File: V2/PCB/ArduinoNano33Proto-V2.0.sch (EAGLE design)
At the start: 53 parts, among them J1 RJ11, J2 RJ11, J23 455-1750-1-ND, J24 455-1750-1-ND, J26 455-1750-1-ND, J27 455-1750-1-ND, J31 455-1750-1-ND, J32 455-1750-1-ND, J38 455-1750-1-ND, J39 455-1750-1-ND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

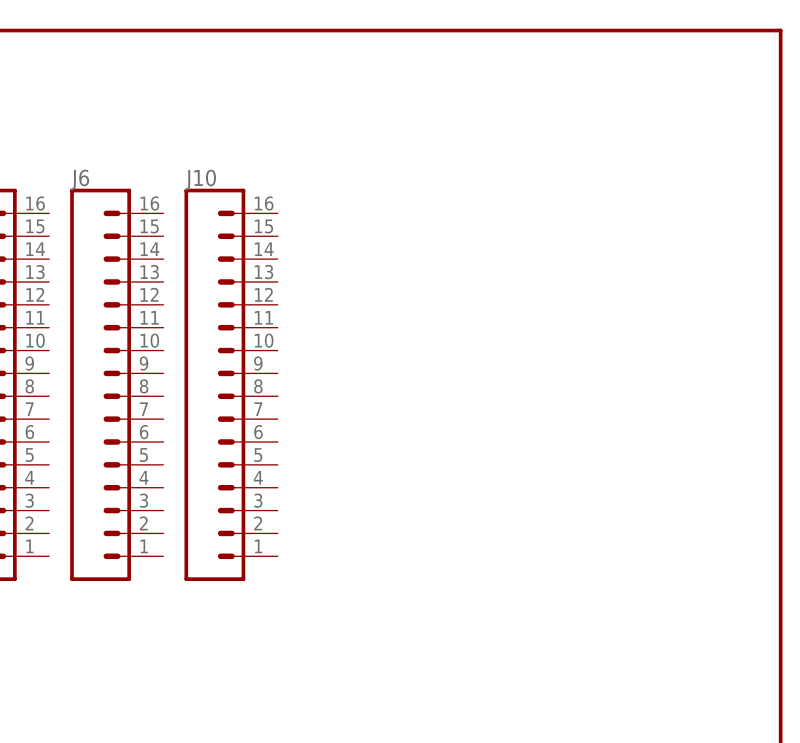
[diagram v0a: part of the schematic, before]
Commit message: Update to V2 (RJ11) board.
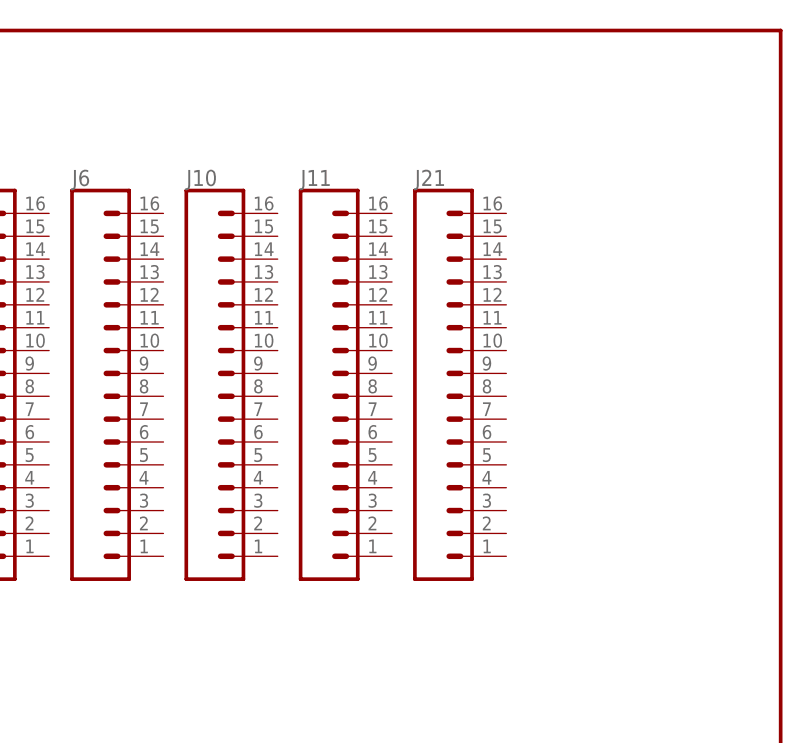
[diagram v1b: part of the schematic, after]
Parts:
- added J11, J21: (no value), SparkFun-Connectors:CONN_161X16_NO_SILK
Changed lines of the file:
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@@
 <part name="J34" library="SparkFun-Connectors" deviceset="CONN_01" device="PTH_NO_SILK_YES_STOP"/>
 <part name="J35" library="SparkFun-Connectors" deviceset="CONN_01" device="PTH_NO_SILK_YES_STOP"/>
+<part name="J11" library="SparkFun-Connectors" deviceset="CONN_16" device="1X16_NO_SILK"/>
+<part name="J21" library="SparkFun-Connectors" deviceset="CONN_16" device="1X16_NO_SILK"/>
 </parts>
 <sheets>
@@
 <instance part="J34" gate="G$1" x="-241.3" y="312.42" rot="R90"/>
 <instance part="J35" gate="G$1" x="-251.46" y="312.42" rot="R90"/>
+<instance part="J11" gate="G$1" x="378.46" y="241.3"/>
+<instance part="J21" gate="G$1" x="391.16" y="241.3"/>
 </instances>
 <busses>
